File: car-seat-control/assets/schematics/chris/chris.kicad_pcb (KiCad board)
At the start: 6 copper layers, 63 x 73.2 mm, 89 parts, among them J1 Battery, J2 Switch, J3 TYPE-C 16PIN, J4 NTC 10k, J5 Conn_01x03_Pin, J6 Conn_01x03_Pin, J7 Peripherals, J8 Charger, J9 Status LED, K1 STKF-12V3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

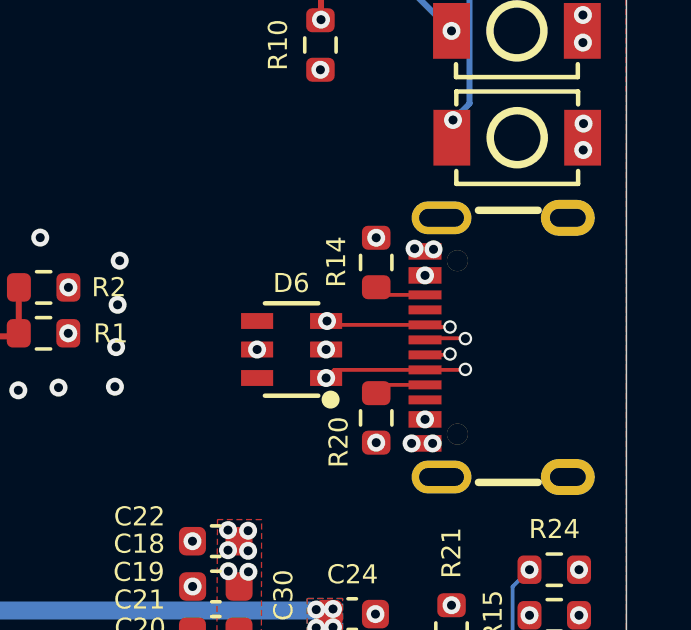
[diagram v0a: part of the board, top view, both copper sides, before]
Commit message: Update assets with newest version of schematics/pcb
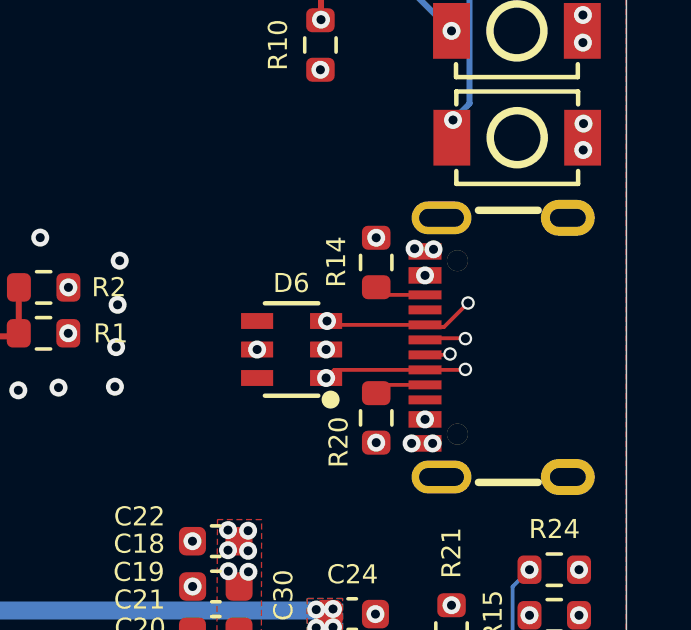
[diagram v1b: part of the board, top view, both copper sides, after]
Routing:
- net /USB_D+: track 20.6 -> 22.6 mm
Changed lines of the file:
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@@
 			(plot_on_all_layers_selection 0x00000000_00000000_00000000_00000000)
 			(disableapertmacros no)
-			(usegerberextensions no)
+			(usegerberextensions yes)
 			(usegerberattributes yes)
 			(usegerberadvancedattributes yes)
-			(creategerberjobfile yes)
+			(creategerberjobfile no)
 			(dashed_line_dash_ratio 12.000000)
 			(dashed_line_gap_ratio 3.000000)
@@
 			(outputformat 1)
 			(mirror no)
-			(drillshape 1)
+			(drillshape 0)
 			(scaleselection 1)
-			(outputdirectory "")
+			(outputdirectory "./")
 		)
 	)
@@
 	)
 	(segment
-		(start 190.4 92.3)
-		(end 189.6375 92.3)
+		(start 189.6375 92.3)
+		(end 189.5675 92.23)
 		(width 0.127)
 		(layer "F.Cu")
@@
 	)
 	(segment
-		(start 186.4 92.23)
-		(end 186.27 92.1)
+		(start 191 91.5)
+		(end 190.2 92.3)
 		(width 0.127)
 		(layer "F.Cu")
@@
 	)
 	(segment
-		(start 189.6375 92.3)
-		(end 189.5675 92.23)
+		(start 190.2 92.3)
+		(end 189.6375 92.3)
+		(width 0.127)
+		(layer "F.Cu")
+		(net 44)
+	)
+	(segment
+		(start 186.4 92.23)
+		(end 186.27 92.1)
 		(width 0.127)
 		(layer "F.Cu")
@@
 	)
 	(via
-		(at 190.4 92.3)
+		(at 191 91.5)
 		(size 0.45)
 		(drill 0.3)
@@
 	)
 	(segment
+		(start 191 91.5)
+		(end 190.348154 92.151846)
+		(width 0.127)
+		(layer "In3.Cu")
+		(net 44)
+	)
+	(segment
 		(start 184.903159 92.1)
 		(end 182.538501 89.735342)
@@
 	)
 	(segment
-		(start 190.348154 92.351846)
-		(end 190.4 92.3)
+		(start 190.348154 92.151846)
+		(end 190.348154 93.148154)
 		(width 0.127)
 		(layer "In3.Cu")
@@
 	(segment
 		(start 190.348154 93.148154)
-		(end 190.348154 92.351846)
-		(width 0.127)
-		(layer "In3.Cu")
-		(net 44)
-	)
-	(segment
-		(start 190.4 93.2)
-		(end 190.348154 93.148154)
+		(end 190.4 93.2)
 		(width 0.127)
 		(layer "In3.Cu")
